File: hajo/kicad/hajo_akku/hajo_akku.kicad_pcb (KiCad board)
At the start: 2 copper layers, 69.2 x 89.5 mm, 22 parts, among them J1 Seetalk NG, J2 Batteries, J3 Terminator, U1 MCP2562, U2 LF50CV

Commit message: fix boards
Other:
- outline, holes or cut-outs redrawn
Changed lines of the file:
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@@
         (effects (font (size 1 1) (thickness 0.15)))
     )
-    (fp_text value "316K" (at 3.81 2.37) (layer "F.Fab")
-        (effects (font (size 1 1) (thickness 0.15)))
-    )
-    (fp_text user "${REFERENCE}" (at 3.81 0) (layer "F.Fab")
+    (fp_text value "316K" (at 3.302 -0.508) (layer "F.SilkS")
+        (effects (font (size 1 1) (thickness 0.15)))
+    )
+    (fp_text user "${REFERENCE}" (at 5.588 0.635) (layer "F.Fab")
         (effects (font (size 1 1) (thickness 0.15)))
     )
@@
         (effects (font (size 1 1) (thickness 0.15)))
     )
-    (fp_text value "316K" (at 3.81 2.37) (layer "F.Fab")
-        (effects (font (size 1 1) (thickness 0.15)))
-    )
-    (fp_text user "${REFERENCE}" (at 3.81 0) (layer "F.Fab")
+    (fp_text value "316K" (at 3.302 -0.508) (layer "F.SilkS")
+        (effects (font (size 1 1) (thickness 0.15)))
+    )
+    (fp_text user "${REFERENCE}" (at 4.953 0.381) (layer "F.Fab")
         (effects (font (size 1 1) (thickness 0.15)))
     )
@@
         (effects (font (size 1 1) (thickness 0.15)))
     )
-    (fp_text value "316K" (at 3.81 2.37) (layer "F.Fab")
-        (effects (font (size 1 1) (thickness 0.15)))
-    )
-    (fp_text user "${REFERENCE}" (at 3.81 0) (layer "F.Fab")
+    (fp_text value "316K" (at 3.302 -0.508) (layer "F.SilkS")
+        (effects (font (size 1 1) (thickness 0.15)))
+    )
+    (fp_text user "${REFERENCE}" (at 5.08 0.381) (layer "F.Fab")
         (effects (font (size 1 1) (thickness 0.15)))
     )
@@
     (property "ki_keywords" "cap capacitor")
     (attr through_hole)
-    (fp_text reference "C3" (at 2.5 -2.25) (layer "F.SilkS")
-        (effects (font (size 1 1) (thickness 0.15)))
-    )
-    (fp_text value "100n" (at 2.5 2.25) (layer "F.Fab")
+    (fp_text reference "C3" (at -0.167 -2.159) (layer "F.SilkS")
+        (effects (font (size 1 1) (thickness 0.15)))
+    )
+    (fp_text value "100n" (at 4.024 -2.159) (layer "F.SilkS")
         (effects (font (size 1 1) (thickness 0.15)))
     )
@@
         (effects (font (size 1 1) (thickness 0.15)))
     )
-    (fp_text value "16.9K" (at 3.81 2.37) (layer "F.Fab")
-        (effects (font (size 1 1) (thickness 0.15)))
-    )
-    (fp_text user "${REFERENCE}" (at 3.81 0) (layer "F.Fab")
+    (fp_text value "16.9K" (at 4.318 0.635) (layer "F.SilkS")
+        (effects (font (size 1 1) (thickness 0.15)))
+    )
+    (fp_text user "${REFERENCE}" (at 2.413 -0.381) (layer "F.Fab")
         (effects (font (size 1 1) (thickness 0.15)))
     )
@@
     (property "ki_keywords" "cap capacitor")
     (attr through_hole)
-    (fp_text reference "C1" (at 2.5 -2.25) (layer "F.SilkS")
-        (effects (font (size 1 1) (thickness 0.15)))
-    )
-    (fp_text value "100n" (at 2.5 2.25) (layer "F.Fab")
+    (fp_text reference "C1" (at -0.461 -2.25) (layer "F.SilkS")
+        (effects (font (size 1 1) (thickness 0.15)))
+    )
+    (fp_text value "100n" (at 3.603 -2.159) (layer "F.SilkS")
         (effects (font (size 1 1) (thickness 0.15)))
     )
@@
         (effects (font (size 1 1) (thickness 0.15)))
     )
-    (fp_text value "16.9K" (at 3.81 2.37) (layer "F.Fab")
-        (effects (font (size 1 1) (thickness 0.15)))
-    )
-    (fp_text user "${REFERENCE}" (at 3.81 0) (layer "F.Fab")
+    (fp_text value "16.9K" (at 4.191 0.635) (layer "F.SilkS")
+        (effects (font (size 1 1) (thickness 0.15)))
+    )
+    (fp_text user "${REFERENCE}" (at 2.667 -0.381) (layer "F.Fab")
         (effects (font (size 1 1) (thickness 0.15)))
     )
@@
     (property "ki_keywords" "cap capacitor")
     (attr through_hole)
-    (fp_text reference "C5" (at 2.5 -2.169) (layer "F.SilkS")
-        (effects (font (size 1 1) (thickness 0.15)))
-    )
-    (fp_text value "100n" (at 2.5 2.25) (layer "F.Fab")
+    (fp_text reference "C5" (at -0.167 -2.159) (layer "F.SilkS")
+        (effects (font (size 1 1) (thickness 0.15)))
+    )
+    (fp_text value "100n" (at 3.643 -2.159) (layer "F.SilkS")
         (effects (font (size 1 1) (thickness 0.15)))
     )
@@
         (effects (font (size 1 1) (thickness 0.15)))
     )
-    (fp_text value "16.9K" (at 3.81 2.37) (layer "F.Fab")
-        (effects (font (size 1 1) (thickness 0.15)))
-    )
-    (fp_text user "${REFERENCE}" (at 3.81 0) (layer "F.Fab")
+    (fp_text value "16.9K" (at 4.064 0.381) (layer "F.SilkS")
+        (effects (font (size 1 1) (thickness 0.15)))
+    )
+    (fp_text user "${REFERENCE}" (at 2.667 -0.381) (layer "F.Fab")
         (effects (font (size 1 1) (thickness 0.15)))
     )
@@
   (gr_line (start 34.833 74.965) (end 39.913 74.965)
     (stroke (width 0.15) (type default)) (layer "F.SilkS"))
-  (gr_line (start 77.679 12.999) (end 17.499 12.999)
+  (gr_line (start 75.6862 12.999) (end 19.5014 12.999)
     (stroke (width 0.1) (type default)) (layer "Edge.Cuts"))
-  (gr_arc (start 12.999 97.999) (mid 16.180981 99.317019) (end 17.499 102.499)
+  (gr_arc (start 12.999 95.999) (mid 17.595194 97.902806) (end 19.499 102.499)
     (stroke (width 0.1) (type default)) (layer "Edge.Cuts"))
-  (gr_arc (start 17.499 12.999) (mid 16.180981 16.180981) (end 12.999 17.499)
+  (gr_arc (start 19.499 12.999) (mid 17.595194 17.595194) (end 12.999 19.499)
     (stroke (width 0.1) (type default)) (layer "Edge.Cuts"))
-  (gr_arc (start 82.179 17.499) (mid 78.997019 16.180981) (end 77.679 12.999)
+  (gr_arc (start 82.214 19.499) (mid 77.59513 17.607618) (end 75.678906 12.999)
     (stroke (width 0.1) (type default)) (layer "Edge.Cuts"))
-  (gr_line (start 82.179 97.999) (end 82.179 17.499)
+  (gr_line (start 82.179 96.0062) (end 82.214 19.5014)
     (stroke (width 0.1) (type default)) (layer "Edge.Cuts"))
-  (gr_arc (start 77.679 102.499) (mid 78.997019 99.317019) (end 82.179 97.999)
+  (gr_arc (start 75.679 102.4832) (mid 77.588382 97.89721) (end 82.179 95.998981)
     (stroke (width 0.1) (type default)) (layer "Edge.Cuts"))
-  (gr_line (start 12.999 17.499) (end 12.999 97.999)
+  (gr_line (start 12.999 19.5014) (end 12.999 96.0062)
     (stroke (width 0.1) (type default)) (layer "Edge.Cuts"))
-  (gr_line (start 17.499 102.499) (end 77.679 102.499)
+  (gr_line (start 19.5014 102.499) (end 75.6862 102.4832)
     (stroke (width 0.1) (type default)) (layer "Edge.Cuts"))
   (gr_text "12V" (at 20.482 76.362) (layer "F.SilkS")

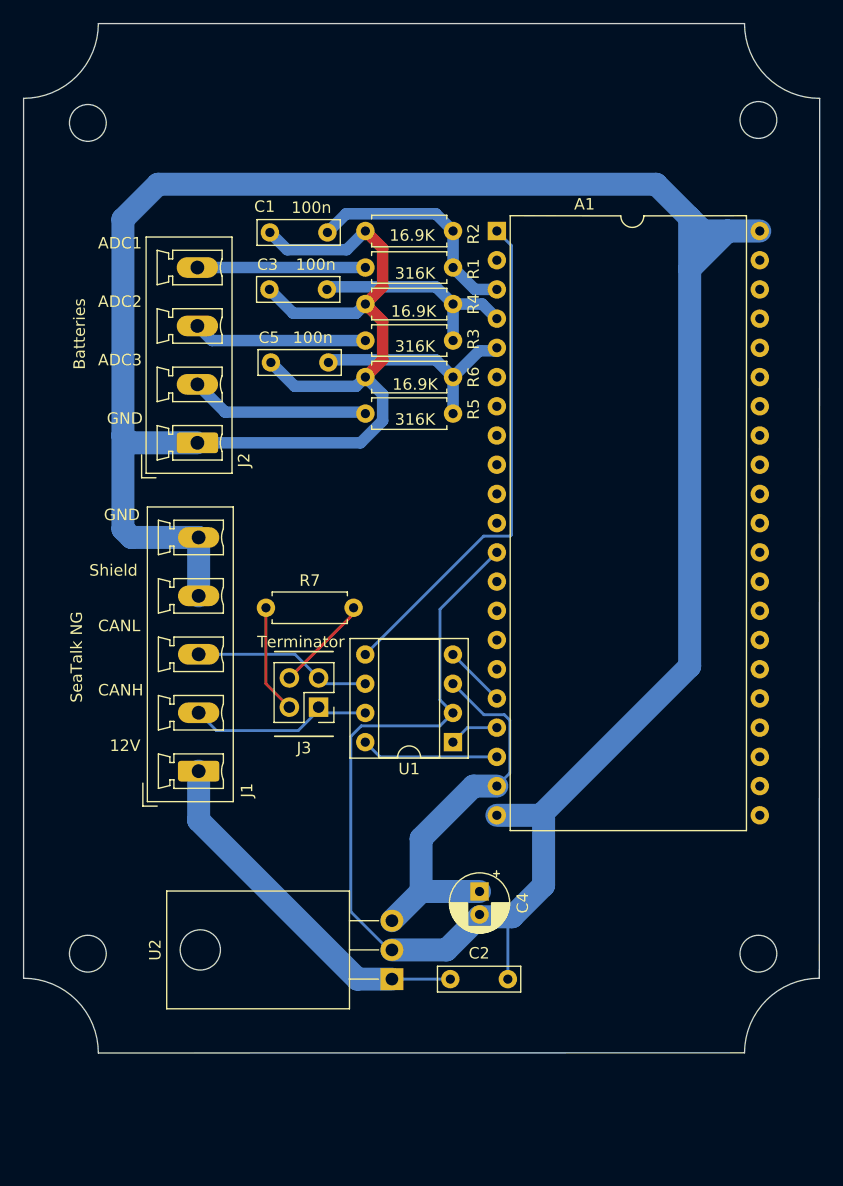
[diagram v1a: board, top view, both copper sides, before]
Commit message: akku on new board
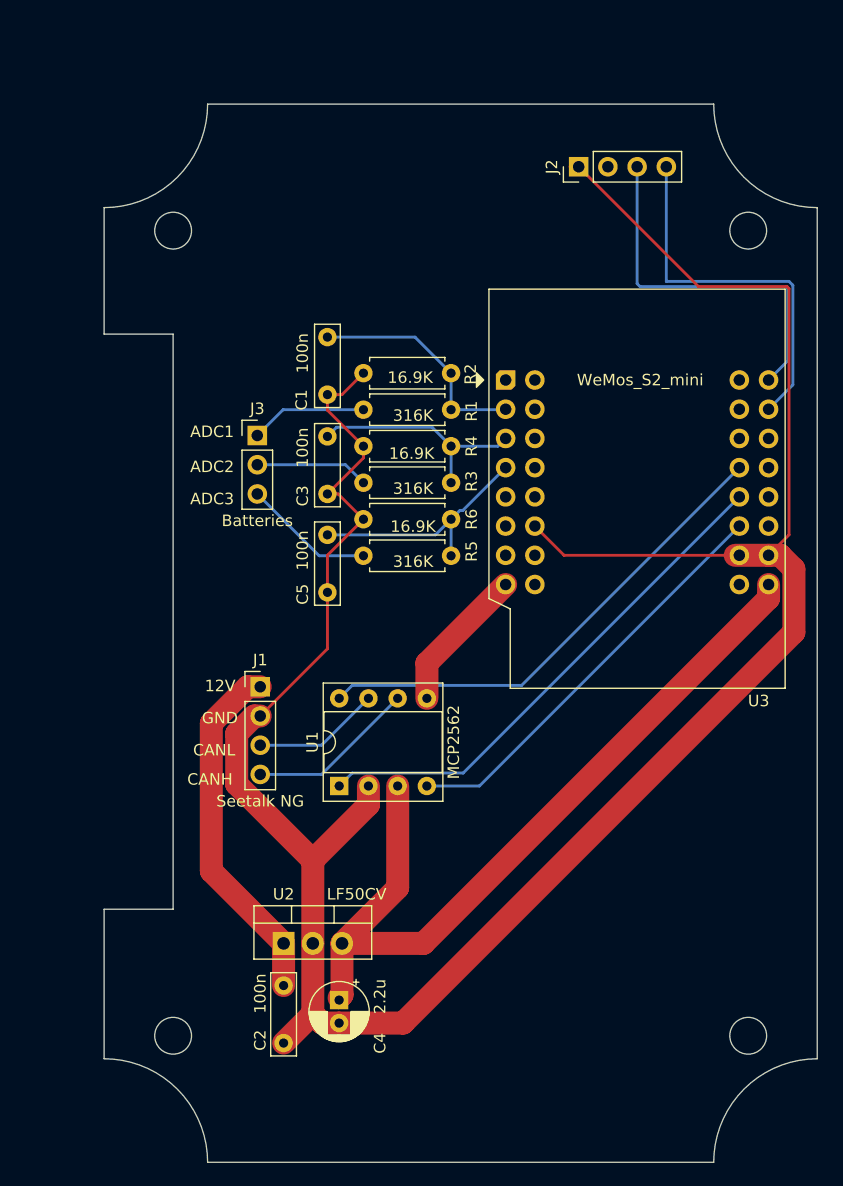
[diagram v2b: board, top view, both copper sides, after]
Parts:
- removed A1: ESP32-S2_Mini-2, own:DIP-42_W15.24mm
- removed R7: 120, Resistor_THT:R_Axial_DIN0207_L6.3mm_D2.5mm_P7.62mm_Horizontal
- added U3: WeMos_S2_mini, own:WEMOS_S2_mini_traced, F.Cu at (54.9, 44.0)
- J1: footprint Connector_Phoenix_MC_HighVoltage:PhoenixContact_MCV_1,5_5-G-5.08_1x05_P5.08mm_Vertical -> Connector_PinHeader_2.54mm:PinHeader_1x04_P2.54mm_Vertical
- J2: value Batteries -> Debug; footprint Connector_Phoenix_MC_HighVoltage:PhoenixContact_MCV_1,5_4-G-5.08_1x04_P5.08mm_Vertical -> Connector_PinHeader_2.54mm:PinHeader_1x04_P2.54mm_Vertical
- J3: value Terminator -> Batteries; footprint Connector_PinHeader_2.54mm:PinHeader_2x02_P2.54mm_Vertical -> Connector_PinHeader_2.54mm:PinHeader_1x03_P2.54mm_Vertical
- U2: footprint Package_TO_SOT_THT:TO-220-3_Horizontal_TabDown -> Package_TO_SOT_THT:TO-220-3_Vertical
- moved H3 58.2 mm to (76.0, 31.0)
- moved H1 51.8 mm to (26.0, 31.0)
- moved J2 40.9 mm to (61.3, 25.4)
- moved J3 24.2 mm to (33.3, 48.8), turned to 0 degrees
- moved C5 20.6 mm to (39.4, 62.5), turned to 90 degrees
- moved C3 18.5 mm to (39.4, 53.9), turned to 90 degrees
- moved C4 15.4 mm to (40.4, 97.9)
- moved C1 15.0 mm to (39.4, 45.3), turned to 90 degrees
- moved C2 14.5 mm to (35.6, 96.6), turned to -90 degrees
- moved R6 12.4 mm to (42.5, 56.1)
- moved R1 12.4 mm to (50.2, 46.6)
- moved R2 12.4 mm to (42.5, 43.4)
- moved R3 12.4 mm to (50.2, 52.9)
- moved R4 12.4 mm to (42.5, 49.7)
- moved R5 12.4 mm to (50.2, 59.3)
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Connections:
- J1 pad 2: /CANH -> GND
- J1 pad 3: /CANL -> /CANH
- J1 pad 4: GND -> /CANL
- J2 pad 2: Net-(J2-Pin_2) -> unconnected-(J2-Pin_2-Pad2)
- J2 pad 3: Net-(J2-Pin_3) -> /DebugTX
- J2 pad 4: Net-(J2-Pin_4) -> /DebugRX
- J3 pad 1: /CANH -> Net-(J3-Pin_1)
- J3 pad 3: /CANL -> Net-(J3-Pin_3)
- R1 pad 2: Net-(J2-Pin_4) -> Net-(J3-Pin_1)
- R3 pad 2: Net-(J2-Pin_3) -> Net-(J3-Pin_2)
- R5 pad 2: Net-(J2-Pin_2) -> Net-(J3-Pin_3)
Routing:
- net GND: track 308.5 -> 217.9 mm
- net /TXD: track 4.34 -> 45.2 mm
- net +5V: track 34.2 -> 71.2 mm
- net /DebugRX: track 0.00 -> 32.8 mm
- net /DebugTX: track 0.00 -> 32.1 mm
- net +3.3V: track 44.0 -> 12.7 mm
- net /STBY: track 12.0 -> 43.1 mm
- net /RXD: track 5.40 -> 36.5 mm
- net Net-(J2-Pin_2): track 15.7 -> 0.00 mm
- net Net-(J2-Pin_3): track 15.1 -> 0.00 mm
- net Net-(J2-Pin_4): track 14.6 -> 0.00 mm
- net Net-(J3-Pin_3): track 0.00 -> 11.5 mm
- net Net-(J3-Pin_1): track 0.00 -> 10.2 mm
- net Net-(J3-Pin_4): track 8.41 -> 0.00 mm
- net /CANH: track 16.3 -> 11.1 mm
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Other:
- board size 69.2 x 89.5 mm -> 62 x 92 mm
- board text removed: "Batteries"
- board text removed: "SeaTalk NG"
- board text removed: "Shield"
- board text removed: "Terminator"

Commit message: pcv rework
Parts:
- moved C1 4.46 mm to (38.3, 40.9)
- moved C5 3.80 mm to (37.9, 59.0), turned to -90 degrees
- moved R2 2.25 mm to (42.5, 41.1)
- moved R1 2.17 mm to (50.1, 44.4)
- moved C3 1.39 mm to (38.1, 53.4)
- moved J3 0.37 mm to (33.6, 48.6)
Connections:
- J2 pad 3: /DebugTX -> /DebugRX
- J2 pad 4: /DebugRX -> /DebugTX
- U1 pad 8: /STBY -> GND
- U3 pad 15: /DebugRX -> unconnected-(U3-GPIO37-Pad15)
- U3 pad 17: unconnected-(U3-GPIO1-Pad17) -> GND
- U3 pad 22: GND -> unconnected-(U3-GPIO10-Pad22)
- U3 pad 29: /STBY -> unconnected-(U3-GPIO34-Pad29)
- U3 pad 32: unconnected-(U3-GPIO40-Pad32) -> /DebugRX
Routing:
- net /STBY: track 43.1 -> 0.00 mm
- net GND: track 217.9 -> 247.4 mm
- net /ADC3: track 21.1 -> 24.6 mm
- net /ADC1: track 20.0 -> 22.9 mm
- net /DebugTX: track 32.1 -> 29.6 mm
- net /ADC2: track 20.0 -> 21.5 mm
- net /DebugRX: track 32.8 -> 33.9 mm
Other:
- outline, holes or cut-outs redrawn
- board text added: "NC"
- board text added: "RXD"
- board text added: "TXD"
